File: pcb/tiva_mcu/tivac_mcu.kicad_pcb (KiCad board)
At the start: 2 copper layers, 170.2 x 170.2 mm, 23 parts, among them J1 USB Power, J2 3.5mm TRS Jack, J3 1x3 Header, J4 DE15HD, J5 Monotron_Bridge_MCU_Side, U1 TM4C123G_Launchpad

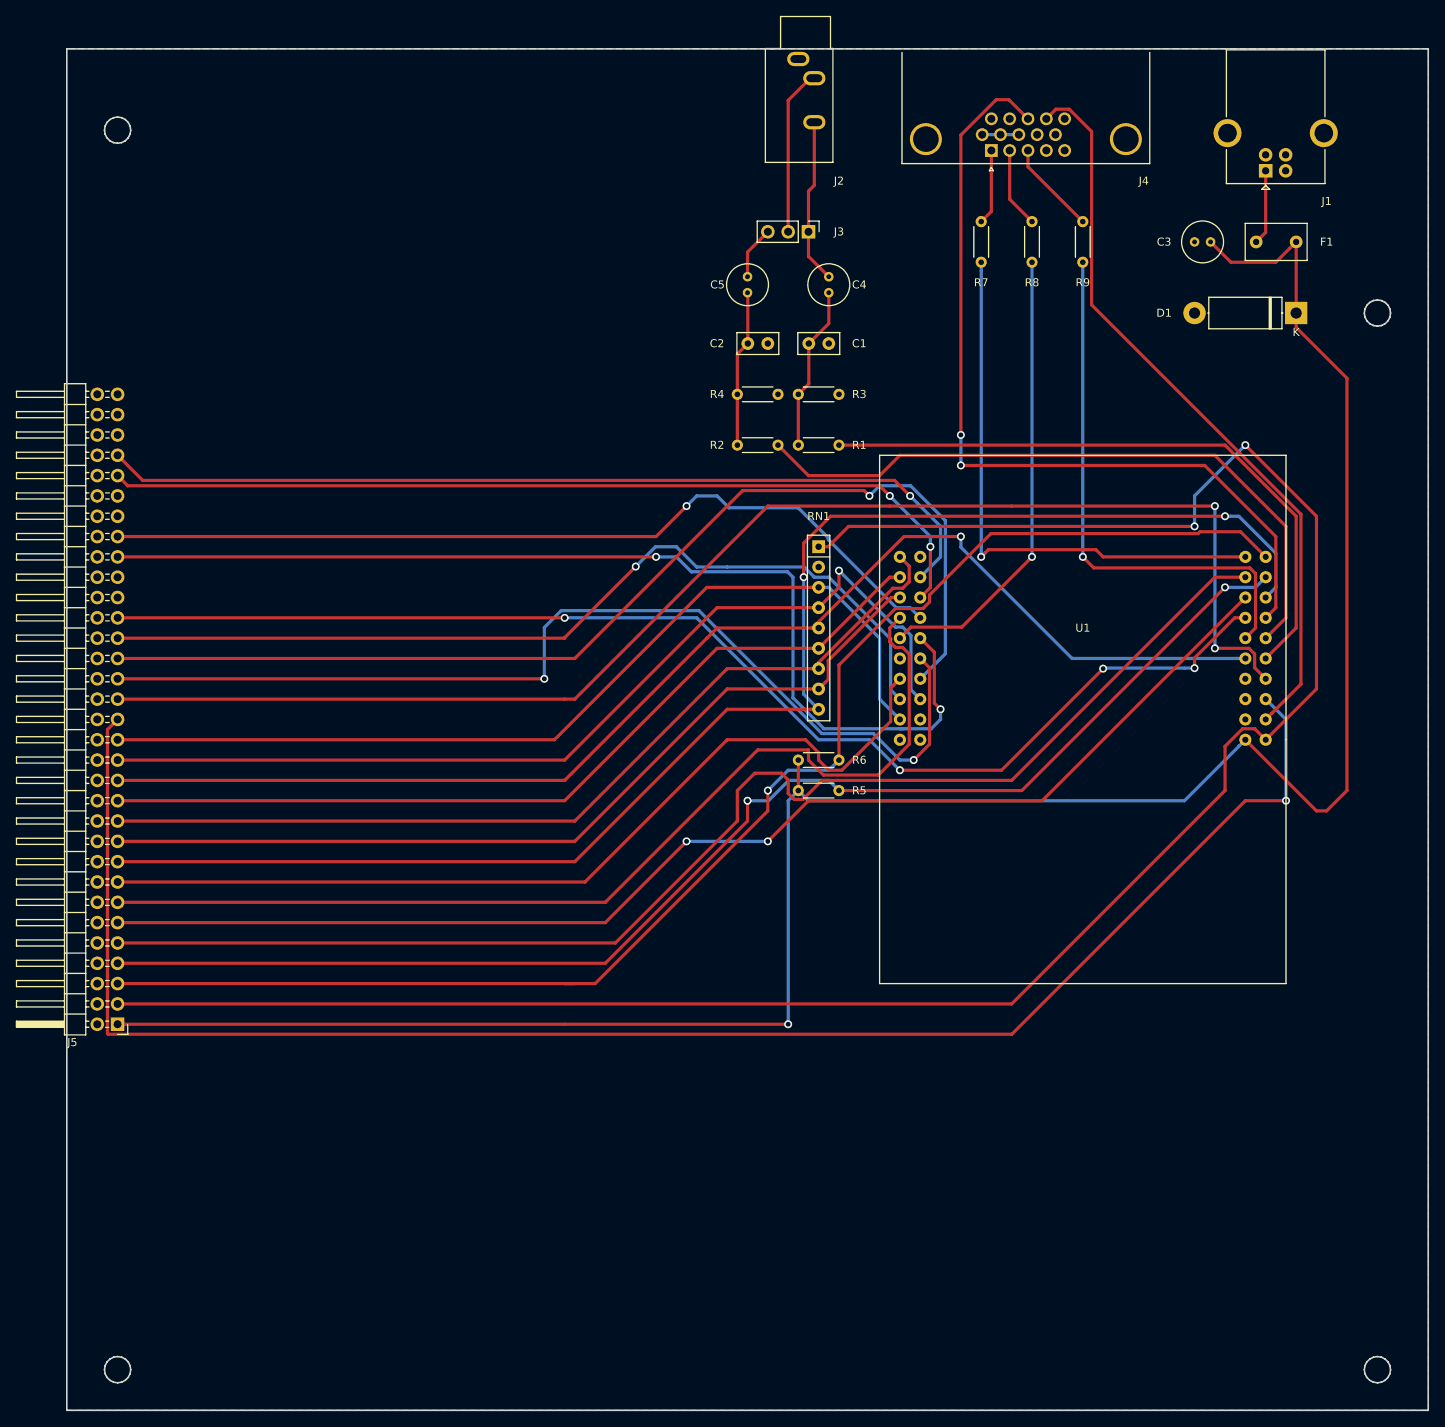
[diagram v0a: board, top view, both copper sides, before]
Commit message: Cleaned up Tiva-C MCU board layout.
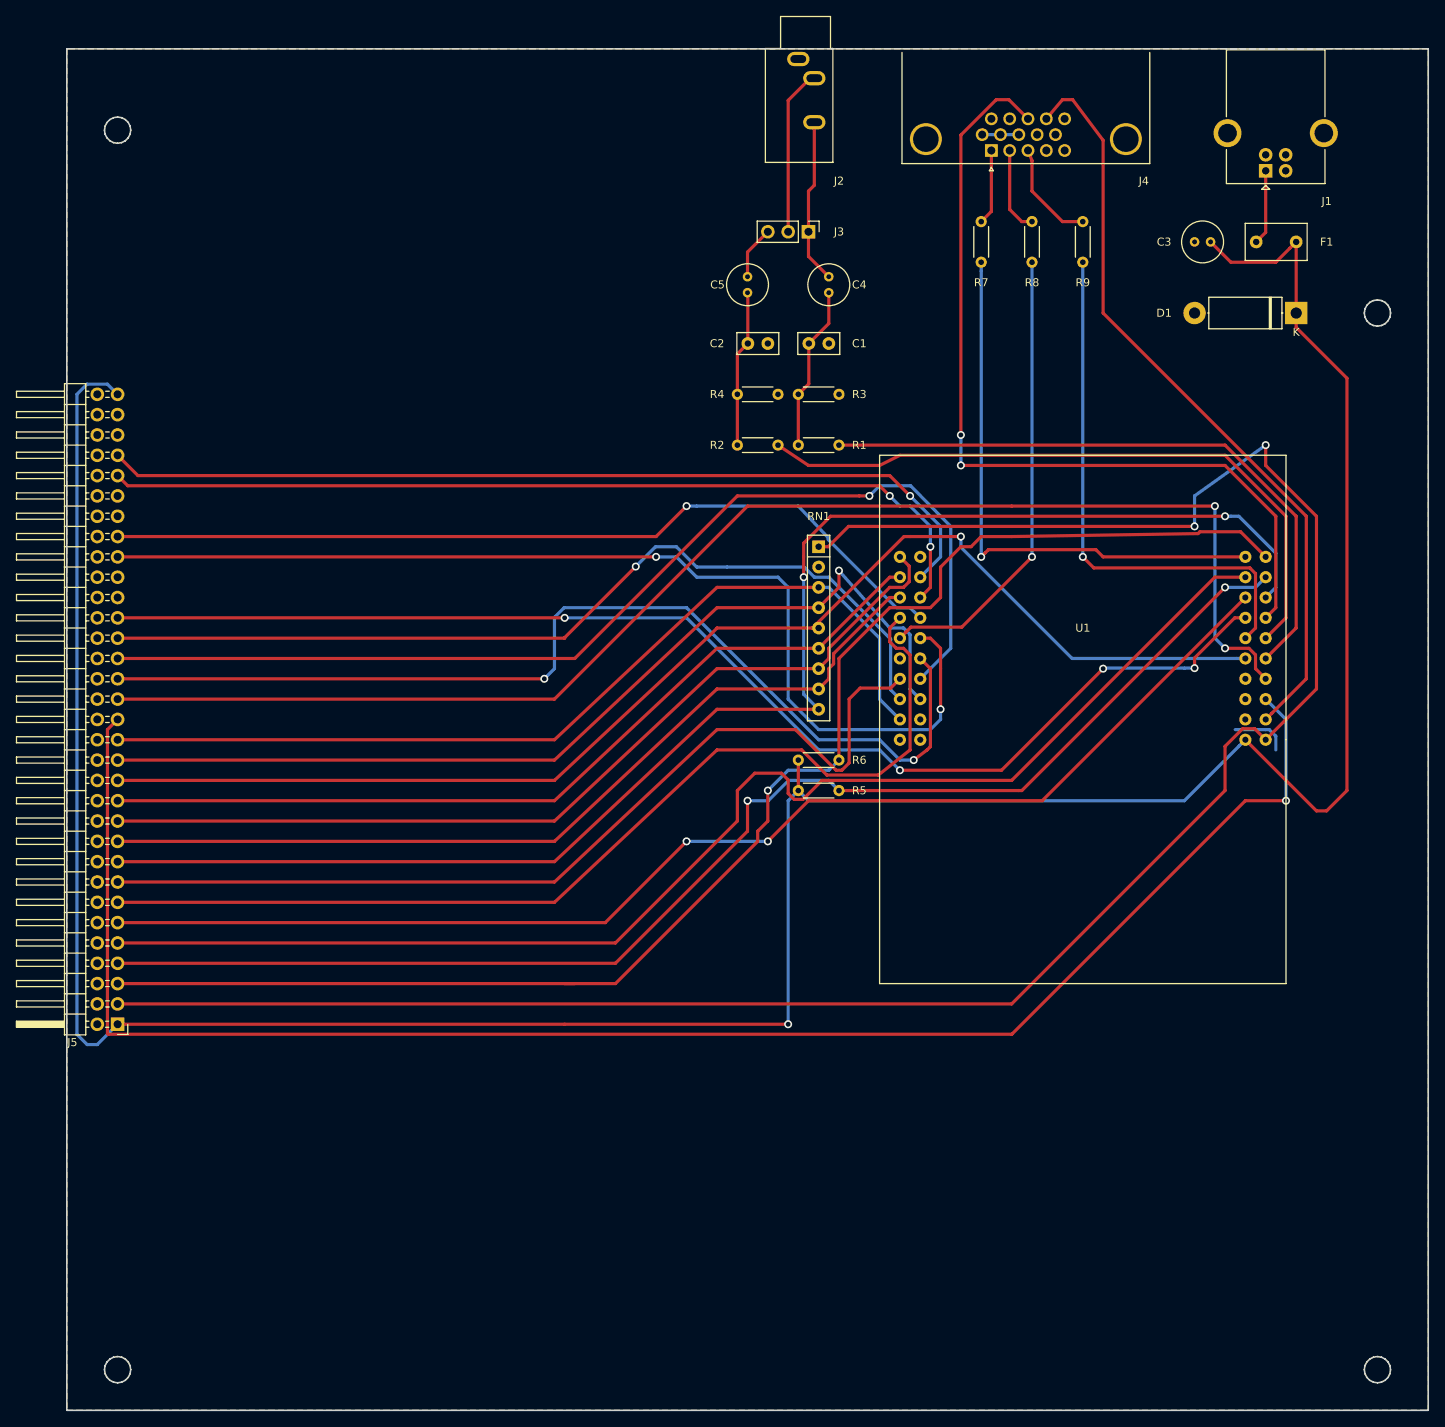
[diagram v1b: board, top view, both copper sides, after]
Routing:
- net +5V: track 278.4 -> 371.2 mm
- net GND: track 4.58 -> 11.7 mm
- net /I2C_SDA: track 178.4 -> 182.0 mm
- net /IRQ_D: track 114.4 -> 116.8 mm
- net /PB5_VGA_VSYNC: track 93.5 -> 95.8 mm
- net /PB4_VGA_HSYNC: track 106.2 -> 107.7 mm
- net Net-(J4-Pad3): track 11.7 -> 13.1 mm
- net /UARTC_TX: track 108.9 -> 107.9 mm
- net +3V3: track 265.5 -> 266.4 mm
- net /PE5_AUDIO_R: track 84.8 -> 84.0 mm
- net /UARTA_TX: track 173.9 -> 173.1 mm
- net /UARTD_RX: track 112.9 -> 113.6 mm
- net /I2C_SCL: track 166.0 -> 166.8 mm
- net Net-(J4-Pad2): track 10.0 -> 10.8 mm
- net /IRQ_C: track 128.3 -> 127.6 mm
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- added copper zone on F.Cu, net GND

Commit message: Working on new PCB design - ATX format.
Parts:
- J5: footprint Connector_PinHeader_2.54mm:PinHeader_2x32_P2.54mm_Horizontal -> Connector_PinSocket_2.54mm:PinSocket_2x24_P2.54mm_Horizontal
- moved J5 34.9 mm to (38.1, 113.0), turned to 0 degrees
- moved U1 32.4 mm to (154.3, 132.7), turned to 0 degrees
- moved RN1 21.1 mm to (103.5, 101.6)
- moved R6 19.2 mm to (106.0, 125.1)
- moved R5 18.8 mm to (101.0, 128.3)
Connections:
- net Net-(J4-Pad3) renamed /BLU
- C4 pad 2: Net-(C4-Pad2) -> /AUD_L
- J2 pad R: Net-(C4-Pad2) -> /AUD_L
- J2 pad T: Net-(J2-PadT) -> /AUD_R
- J3 pad 1: Net-(C4-Pad2) -> /AUD_L
- J3 pad 2: Net-(J2-PadT) -> /AUD_R
- J4 pad 1: Net-(J4-Pad1) -> /RED
- J4 pad 2: Net-(J4-Pad2) -> /GRN
- J5 pad 10: GND -> /IRQ_B
- J5 pad 11: /IRQ_B -> /IRQ_C
- J5 pad 12: GND -> /IRQ_D
- J5 pad 13: /IRQ_C -> /SPI_MOSI
- J5 pad 14: GND -> /SPI_MISO
- J5 pad 15: /IRQ_D -> /SPI_CLK
- J5 pad 17: /SPI_MOSI -> /SPI_CS0
- J5 pad 18: GND -> /SPI_CS1
- J5 pad 19: /SPI_MISO -> /SPI_CS2
- J5 pad 20: GND -> /SPI_CS3
- J5 pad 21: /SPI_CLK -> /UARTA_RX
- J5 pad 22: GND -> /UARTA_TX
- J5 pad 23: /SPI_CS0 -> /UARTA_CTS
- J5 pad 24: GND -> /UARTA_RTS
- J5 pad 25: /SPI_CS1 -> /UARTB_RX
- J5 pad 26: GND -> /UARTB_TX
- J5 pad 27: /SPI_CS2 -> GND
- J5 pad 28: GND -> Net-(J5-Pad28)
- J5 pad 29: /SPI_CS3 -> /UARTC_RX
- J5 pad 3: +3V3 -> +5V
- J5 pad 30: GND -> /UARTC_TX
- J5 pad 31: /UARTA_RX -> GND
- J5 pad 32: GND -> Net-(J5-Pad32)
- J5 pad 33: /UARTA_TX -> /UARTD_RX
- J5 pad 34: GND -> /UARTD_TX
- J5 pad 35: /UARTA_CTS -> GND
- J5 pad 36: GND -> Net-(J5-Pad36)
- J5 pad 37: /UARTA_RTS -> /RED
- J5 pad 39: /UARTB_RX -> GND
- J5 pad 41: /UARTB_TX -> /GRN
- J5 pad 42: GND -> (no net)
- J5 pad 43: GND -> /PB4_VGA_HSYNC
- J5 pad 44: GND -> /PB5_VGA_VSYNC
- J5 pad 45: Net-(J5-Pad45) -> /AUD_L
- J5 pad 47: /UARTC_RX -> /AUD_R
- J5 pad 5: /I2C_SDA -> +3V3
- J5 pad 7: /I2C_SCL -> /I2C_SDA
- J5 pad 8: GND -> /I2C_SCL
- R7 pad 1: Net-(J4-Pad1) -> /RED
- R8 pad 1: Net-(J4-Pad2) -> /GRN
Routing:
- net +5V: track 371.2 -> 23.5 mm, vias 1 -> 0
- net +3V3: track 266.4 -> 0.00 mm, vias 2 -> 0
- net /UARTA_RX: track 213.0 -> 0.00 mm, vias 1 -> 0
- net /SPI_MOSI: track 185.1 -> 0.00 mm, vias 2 -> 0
- net /I2C_SDA: track 182.0 -> 0.00 mm, vias 1 -> 0
- net /UARTA_TX: track 173.1 -> 0.00 mm, vias 2 -> 0
- net /I2C_SCL: track 166.8 -> 0.00 mm, vias 2 -> 0
- net /IRQ_A: track 165.8 -> 0.00 mm
- net /SPI_CS1: track 161.9 -> 0.00 mm, vias 1 -> 0
- net /IRQ_B: track 157.8 -> 0.00 mm, vias 2 -> 0
- net /UARTB_TX: track 157.5 -> 0.00 mm, vias 4 -> 0
- net /UARTA_RTS: track 135.8 -> 0.00 mm, vias 1 -> 0
- net /UARTC_RX: track 132.3 -> 0.00 mm, vias 2 -> 0
- net /UARTA_CTS: track 129.1 -> 0.00 mm, vias 2 -> 0
- net /IRQ_C: track 127.6 -> 0.00 mm
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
